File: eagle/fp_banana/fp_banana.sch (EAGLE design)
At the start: 9 parts, among them J1 CT3149-0, J2 CT3149-2, J3 CT3149-0, J4 CT3149-2, J5 TSM-105-01-S-SV

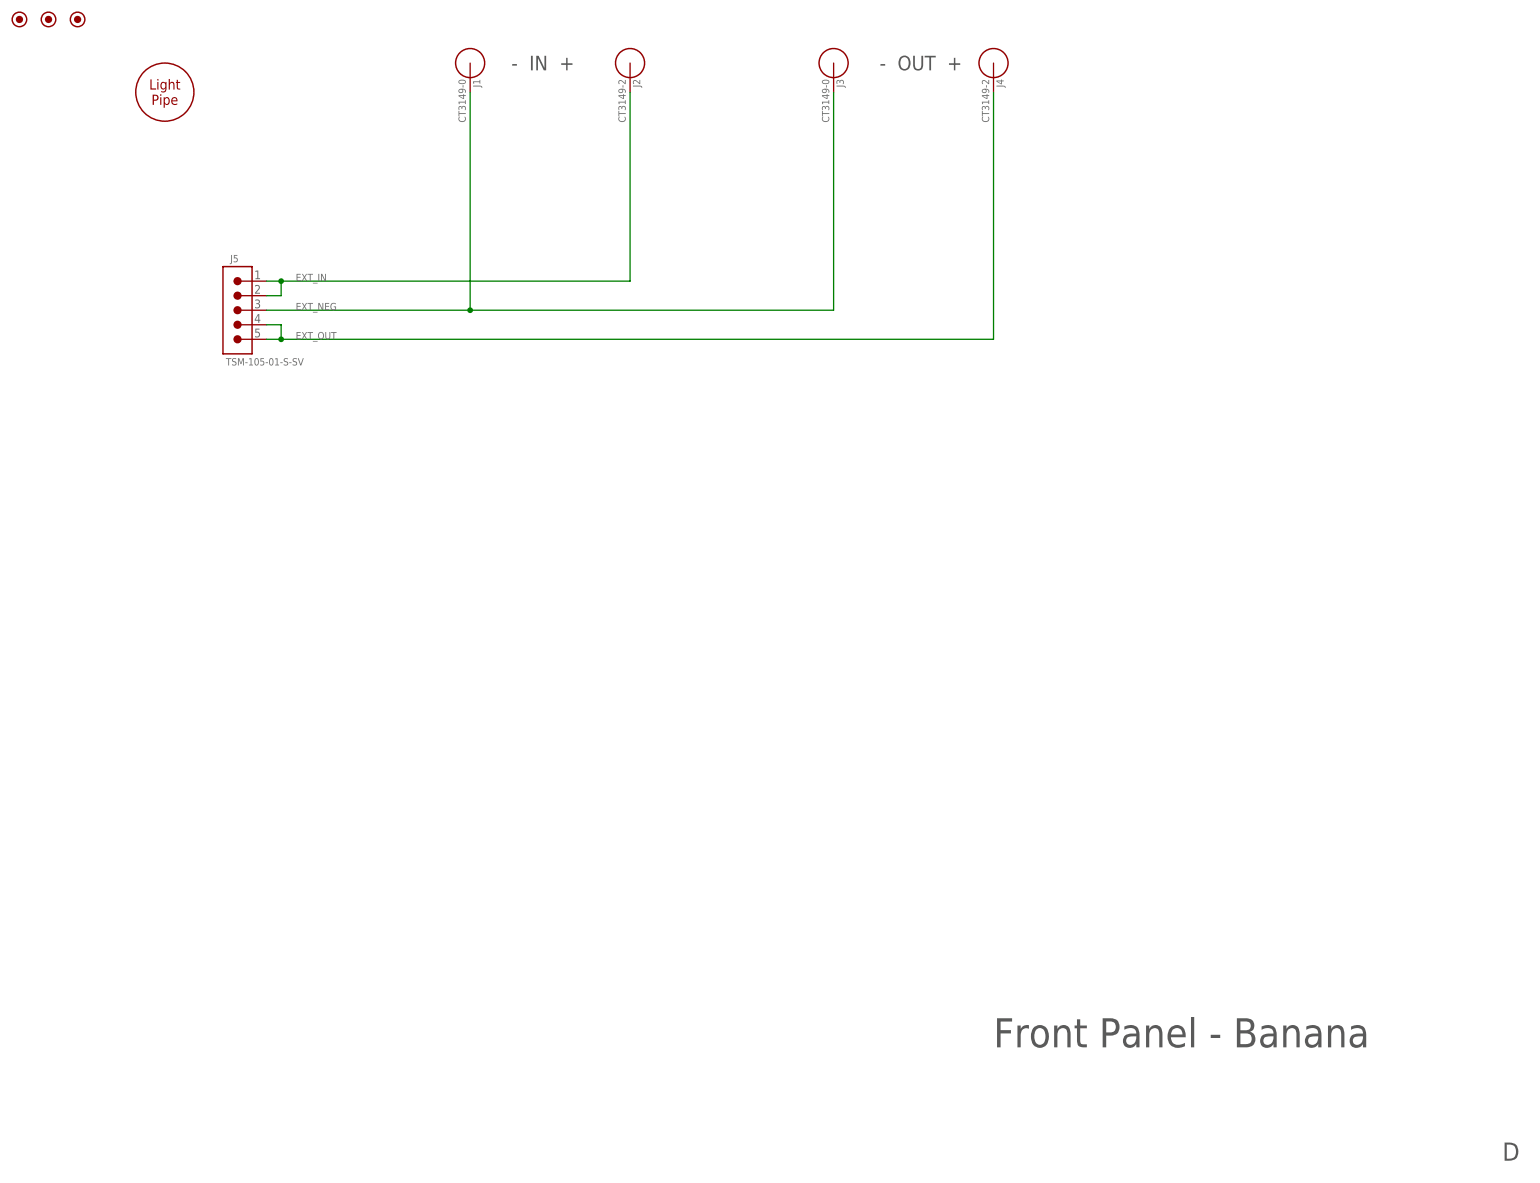
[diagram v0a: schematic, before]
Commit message: Pre-production update.
* Increased clearances from chassis/enclosure ground.
* Improved text.
* Added gerbers.
* Added USB back panel.
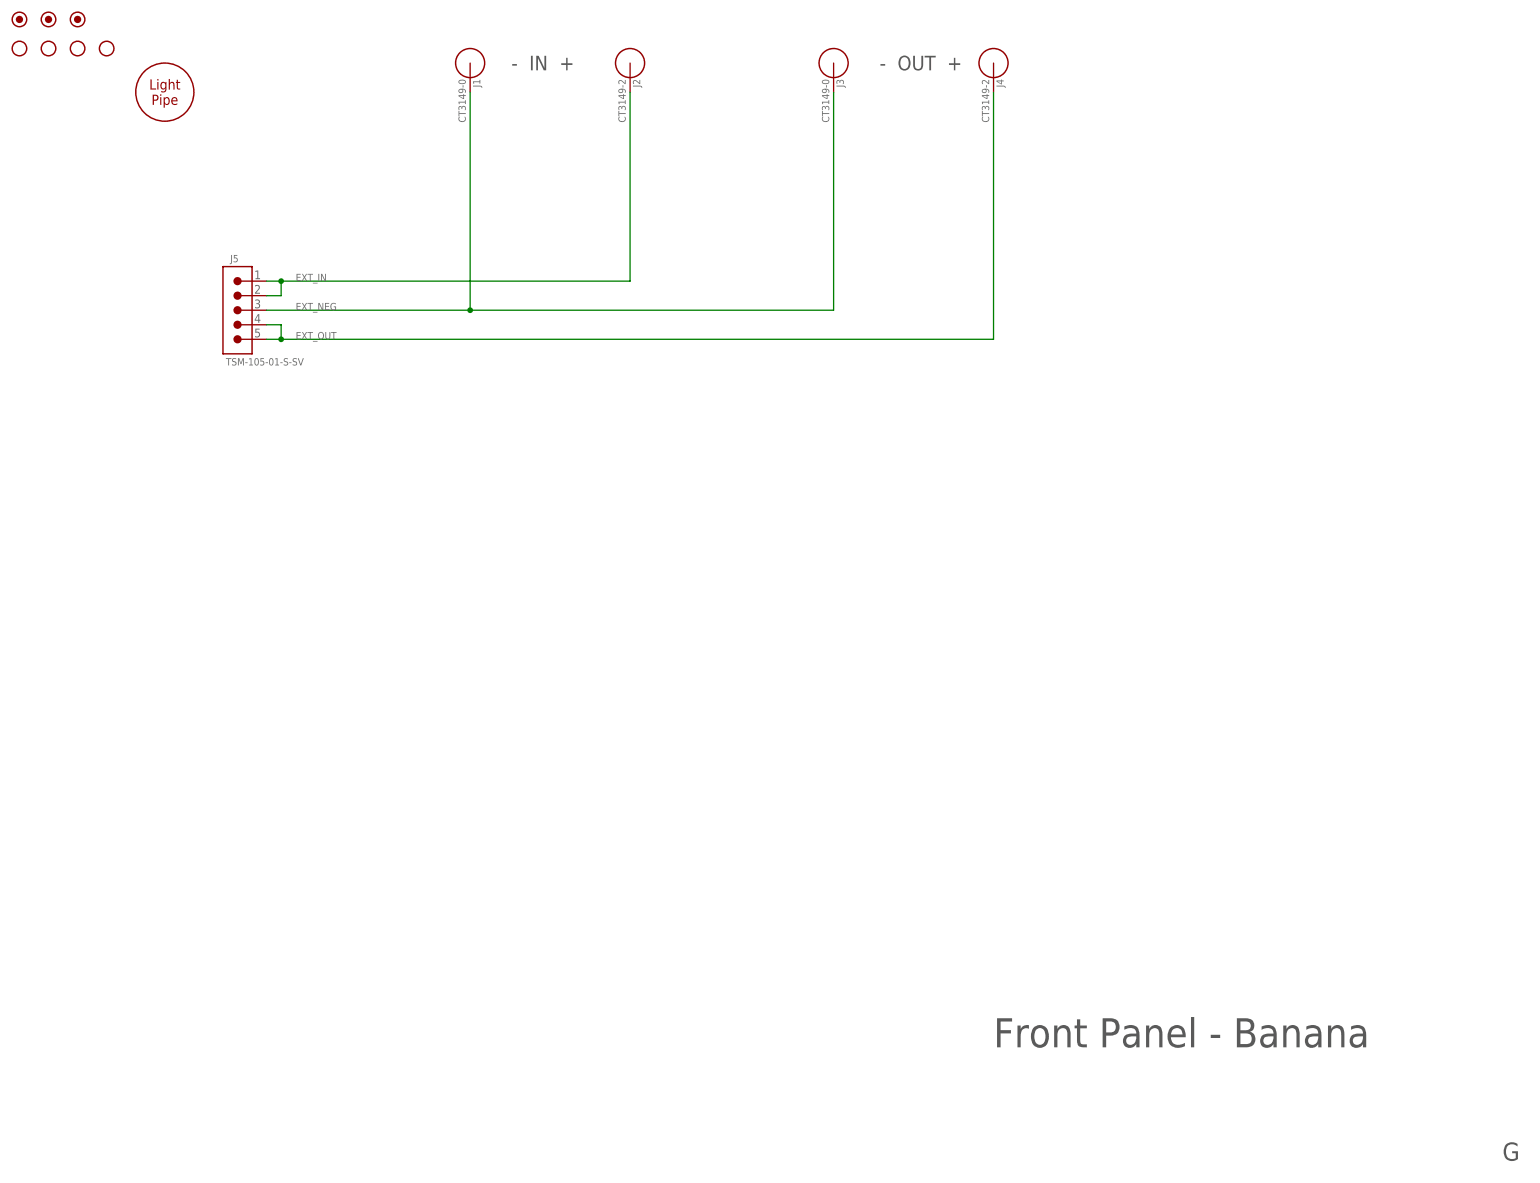
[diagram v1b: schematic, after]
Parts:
- added H2, H3, H4, H5: HOLE_#6, jetperch:HOLE_#6
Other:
- note added: "G"
- note removed: "D"
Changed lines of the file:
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@@
 <?xml version="1.0" encoding="utf-8"?>
 <!DOCTYPE eagle SYSTEM "eagle.dtd">
-<eagle version="9.2.2">
+<eagle version="9.3.2">
 <drawing>
 <settings>
@@
 <part name="FUD2" library="jetperch" deviceset="FIDUCIAL" device="_1MM"/>
 <part name="FUD3" library="jetperch" deviceset="FIDUCIAL" device="_1MM"/>
+<part name="H2" library="jetperch" deviceset="HOLE" device="_#6"/>
+<part name="H3" library="jetperch" deviceset="HOLE" device="_#6"/>
+<part name="H4" library="jetperch" deviceset="HOLE" device="_#6"/>
+<part name="H5" library="jetperch" deviceset="HOLE" device="_#6"/>
 </parts>
 <sheets>
@@
 <plain>
 <text x="177.8" y="26.162" size="5.08" layer="97">Front Panel - Banana</text>
-<text x="266.7" y="6.35" size="3.175" layer="97">D</text>
+<text x="266.7" y="6.35" size="3.175" layer="97">G</text>
 <text x="99.06" y="198.12" size="2.54" layer="97" align="center">-  IN  +</text>
 <text x="165.1" y="198.12" size="2.54" layer="97" align="center">-  OUT  +</text>
@@
 <instance part="FUD2" gate="G$1" x="12.7" y="205.74" smashed="yes"/>
 <instance part="FUD3" gate="G$1" x="17.78" y="205.74" smashed="yes"/>
+<instance part="H2" gate="G$1" x="7.62" y="200.66" smashed="yes"/>
+<instance part="H3" gate="G$1" x="12.7" y="200.66" smashed="yes"/>
+<instance part="H4" gate="G$1" x="17.78" y="200.66" smashed="yes"/>
+<instance part="H5" gate="G$1" x="22.86" y="200.66" smashed="yes"/>
 </instances>
 <busses>

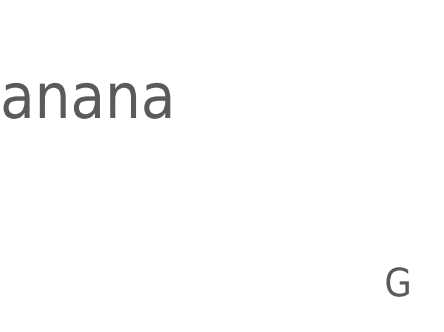
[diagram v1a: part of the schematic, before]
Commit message: Banana Jack front panel rev H
* Increased 5x1 connector pad width from 45 mil to 50 mil.
* Added brief fab notes & fab drawing.
* Improved dimensioning for clarity.
* Removed excessive number of EXT_NEG vias.
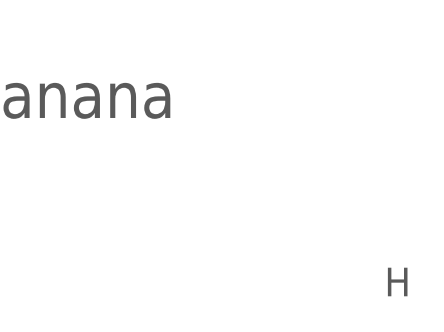
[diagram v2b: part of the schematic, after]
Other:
- note added: "H"
- note removed: "G"
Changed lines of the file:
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@@
 <?xml version="1.0" encoding="utf-8"?>
 <!DOCTYPE eagle SYSTEM "eagle.dtd">
-<eagle version="9.3.2">
+<eagle version="9.5.0">
 <drawing>
 <settings>
@@
 <plain>
 <text x="177.8" y="26.162" size="5.08" layer="97">Front Panel - Banana</text>
-<text x="266.7" y="6.35" size="3.175" layer="97">G</text>
+<text x="266.7" y="6.35" size="3.175" layer="97">H</text>
 <text x="99.06" y="198.12" size="2.54" layer="97" align="center">-  IN  +</text>
 <text x="165.1" y="198.12" size="2.54" layer="97" align="center">-  OUT  +</text>
